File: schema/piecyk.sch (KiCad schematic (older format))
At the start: 29 parts, among them IC1 ATMEGA8-AI, P1 PWR_IN, P2 PWR_OUT, P3 CONN_01X04, P4 CONN_01X04, P5 ISP_IDC, Q1 2N7002, Q2 2N7002, Q3 BC516, SW1 SW_edit, SW2 SW_up, SW3 SW_down, U1 78L05, U2 LM35, U3 HD44780

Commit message: Add 10uF capacitor, optimalize PCB layout
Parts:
- added C3: 10u, Capacitors_Tantalum_SMD:TantalC_SizeA_EIA-3216_HandSoldering, symbol CAPAPOL
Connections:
- net +5V: now also C3.1
- net GND: now also C3.2
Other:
- moved on the sheet: C2
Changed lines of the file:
@@
 $EndComp
 $Comp
-L GND #PWR11
+L GND #PWR01
 U 1 1 52BB03AA
 P 3700 2000
-F 0 "#PWR11" H 3700 2000 30  0001 C CNN
+F 0 "#PWR01" H 3700 2000 30  0001 C CNN
 F 1 "GND" H 3700 1930 30  0001 C CNN
 F 2 "" H 3700 2000 60  0000 C CNN
@@
 $EndComp
 $Comp
-L GND #PWR4
+L GND #PWR02
 U 1 1 52BB0515
 P 1350 4650
-F 0 "#PWR4" H 1350 4650 30  0001 C CNN
+F 0 "#PWR02" H 1350 4650 30  0001 C CNN
 F 1 "GND" H 1350 4580 30  0001 C CNN
 F 2 "" H 1350 4650 60  0000 C CNN
@@
 $EndComp
 $Comp
-L GND #PWR1
+L GND #PWR03
 U 1 1 52BB0524
 P 1050 4650
-F 0 "#PWR1" H 1050 4650 30  0001 C CNN
+F 0 "#PWR03" H 1050 4650 30  0001 C CNN
 F 1 "GND" H 1050 4580 30  0001 C CNN
 F 2 "" H 1050 4650 60  0000 C CNN
@@
 $EndComp
 $Comp
-L GND #PWR5
+L GND #PWR04
 U 1 1 52BB0533
 P 1550 4650
-F 0 "#PWR5" H 1550 4650 30  0001 C CNN
+F 0 "#PWR04" H 1550 4650 30  0001 C CNN
 F 1 "GND" H 1550 4580 30  0001 C CNN
 F 2 "" H 1550 4650 60  0000 C CNN
@@
 $EndComp
 $Comp
-L GND #PWR10
+L GND #PWR05
 U 1 1 52BB0800
 P 3150 6450
-F 0 "#PWR10" H 3150 6450 30  0001 C CNN
+F 0 "#PWR05" H 3150 6450 30  0001 C CNN
 F 1 "GND" H 3150 6380 30  0001 C CNN
 F 2 "" H 3150 6450 60  0000 C CNN
@@
 $EndComp
 $Comp
-L +12V #PWR9
+L +12V #PWR06
 U 1 1 52D0DF48
 P 2950 950
-F 0 "#PWR9" H 2950 900 20  0001 C CNN
+F 0 "#PWR06" H 2950 900 20  0001 C CNN
 F 1 "+12V" H 2950 1050 30  0000 C CNN
 F 2 "" H 2950 950 60  0000 C CNN
@@
 $EndComp
 $Comp
-L GND #PWR15
+L GND #PWR07
 U 1 1 52D0FAD8
 P 6200 3150
-F 0 "#PWR15" H 6200 3150 30  0001 C CNN
+F 0 "#PWR07" H 6200 3150 30  0001 C CNN
 F 1 "GND" H 6200 3080 30  0001 C CNN
 F 2 "" H 6200 3150 60  0000 C CNN
@@
 $EndComp
 $Comp
-L GND #PWR6
+L GND #PWR08
 U 1 1 5459316E
 P 1750 1450
-F 0 "#PWR6" H 1750 1450 30  0001 C CNN
+F 0 "#PWR08" H 1750 1450 30  0001 C CNN
 F 1 "GND" H 1750 1380 30  0001 C CNN
 F 2 "" H 1750 1450 60  0000 C CNN
@@
 $EndComp
 $Comp
-L GND #PWR24
+L GND #PWR09
 U 1 1 54594AD7
 P 9400 2650
-F 0 "#PWR24" H 9400 2650 30  0001 C CNN
+F 0 "#PWR09" H 9400 2650 30  0001 C CNN
 F 1 "GND" H 9400 2580 30  0001 C CNN
 F 2 "" H 9400 2650 60  0000 C CNN
@@
 L C C2
 U 1 1 52BB0288
-P 4200 1450
-F 0 "C2" H 4200 1550 40  0000 L CNN
-F 1 "100n" H 4206 1365 40  0000 L CNN
-F 2 "Capacitors_SMD:C_0805_HandSoldering" H 4238 1300 30  0000 C CNN
-F 3 "~" H 4200 1450 60  0000 C CNN
-	1    4200 1450
+P 4450 1450
+F 0 "C2" H 4450 1550 40  0000 L CNN
+F 1 "100n" H 4456 1365 40  0000 L CNN
+F 2 "Capacitors_SMD:C_0805_HandSoldering" H 4488 1300 30  0000 C CNN
+F 3 "~" H 4450 1450 60  0000 C CNN
+	1    4450 1450
 	1    0    0    -1
 $EndComp
@@
 	3150 1650 3150 1750
 Wire Wire Line
-	3150 1750 4200 1750
+	3150 1750 4450 1750
 Connection ~ 3700 1750
 Wire Wire Line
@@
 	2950 950  2950 1150
 Wire Wire Line
-	4450 1150 4450 950
-$Comp
-L +5V #PWR12
+	4450 950  4450 1250
+$Comp
+L +5V #PWR010
 U 1 1 548A0516
 P 4450 950
-F 0 "#PWR12" H 4450 1040 20  0001 C CNN
+F 0 "#PWR010" H 4450 1040 20  0001 C CNN
 F 1 "+5V" H 4450 1040 30  0000 C CNN
 F 2 "" H 4450 950 60  0000 C CNN
@@
 LCD_RS
 $Comp
-L +5V #PWR23
+L +5V #PWR011
 U 1 1 548A0D87
 P 9100 2350
-F 0 "#PWR23" H 9100 2440 20  0001 C CNN
+F 0 "#PWR011" H 9100 2440 20  0001 C CNN
 F 1 "+5V" H 9100 2440 30  0000 C CNN
 F 2 "" H 9100 2350 60  0000 C CNN
@@
 $EndComp
 $Comp
-L +5V #PWR3
+L +5V #PWR012
 U 1 1 548A102B
 P 1300 2700
-F 0 "#PWR3" H 1300 2790 20  0001 C CNN
+F 0 "#PWR012" H 1300 2790 20  0001 C CNN
 F 1 "+5V" H 1300 2790 30  0000 C CNN
 F 2 "" H 1300 2700 60  0000 C CNN
@@
 $EndComp
 $Comp
-L GND #PWR13
+L GND #PWR013
 U 1 1 548A1F87
 P 5100 5800
-F 0 "#PWR13" H 5100 5800 30  0001 C CNN
+F 0 "#PWR013" H 5100 5800 30  0001 C CNN
 F 1 "GND" H 5100 5730 30  0001 C CNN
 F 2 "" H 5100 5800 60  0000 C CNN
@@
 	6300 7650 5250 7650
 $Comp
-L +12V #PWR2
+L +12V #PWR014
 U 1 1 548A221E
 P 1300 1300
-F 0 "#PWR2" H 1300 1250 20  0001 C CNN
+F 0 "#PWR014" H 1300 1250 20  0001 C CNN
 F 1 "+12V" H 1300 1400 30  0000 C CNN
 F 2 "" H 1300 1300 60  0000 C CNN
@@
 	8250 5650 8450 5650
 $Comp
-L GND #PWR19
+L GND #PWR015
 U 1 1 548A2843
 P 8250 5800
-F 0 "#PWR19" H 8250 5800 30  0001 C CNN
+F 0 "#PWR015" H 8250 5800 30  0001 C CNN
 F 1 "GND" H 8250 5730 30  0001 C CNN
 F 2 "" H 8250 5800 60  0000 C CNN
@@
 	8250 5800 8250 5650
 $Comp
-L +5V #PWR14
+L +5V #PWR016
 U 1 1 548A2D1F
 P 5150 2750
-F 0 "#PWR14" H 5150 2840 20  0001 C CNN
+F 0 "#PWR016" H 5150 2840 20  0001 C CNN
 F 1 "+5V" H 5150 2840 30  0000 C CNN
 F 2 "" H 5150 2750 60  0000 C CNN
@@
 	8100 4500 8100 5450
 $Comp
-L +12V #PWR18
+L +12V #PWR017
 U 1 1 548A3482
 P 8100 3400
-F 0 "#PWR18" H 8100 3350 20  0001 C CNN
+F 0 "#PWR017" H 8100 3350 20  0001 C CNN
 F 1 "+12V" H 8100 3500 30  0000 C CNN
 F 2 "" H 8100 3400 60  0000 C CNN
@@
 	7150 4850 7150 4950
 $Comp
-L GND #PWR16
+L GND #PWR018
 U 1 1 548A3B00
 P 7150 5550
-F 0 "#PWR16" H 7150 5550 30  0001 C CNN
+F 0 "#PWR018" H 7150 5550 30  0001 C CNN
 F 1 "GND" H 7150 5480 30  0001 C CNN
 F 2 "" H 7150 5550 60  0000 C CNN
@@
 	7950 950  7950 1050
 $Comp
-L GND #PWR17
+L GND #PWR019
 U 1 1 548A6D90
 P 7950 1650
-F 0 "#PWR17" H 7950 1650 30  0001 C CNN
+F 0 "#PWR019" H 7950 1650 30  0001 C CNN
 F 1 "GND" H 7950 1580 30  0001 C CNN
 F 2 "" H 7950 1650 60  0000 C CNN
@@
 $EndComp
 $Comp
-L +5V #PWR20
+L +5V #PWR020
 U 1 1 548A7182
 P 8450 1800
-F 0 "#PWR20" H 8450 1890 20  0001 C CNN
+F 0 "#PWR020" H 8450 1890 20  0001 C CNN
 F 1 "+5V" H 8450 1890 30  0000 C CNN
 F 2 "" H 8450 1800 60  0000 C CNN
@@
 	8450 1800 8450 1950
 $Comp
-L GND #PWR21
+L GND #PWR021
 U 1 1 548A73F6
 P 8450 2650
-F 0 "#PWR21" H 8450 2650 30  0001 C CNN
+F 0 "#PWR021" H 8450 2650 30  0001 C CNN
 F 1 "GND" H 8450 2580 30  0001 C CNN
 F 2 "" H 8450 2650 60  0000 C CNN
@@
 NoConn ~ 9500 1850
 $Comp
-L +5V #PWR22
+L +5V #PWR022
 U 1 1 548A85D9
 P 8800 1050
-F 0 "#PWR22" H 8800 1140 20  0001 C CNN
+F 0 "#PWR022" H 8800 1140 20  0001 C CNN
 F 1 "+5V" H 8800 1140 30  0000 C CNN
 F 2 "" H 8800 1050 60  0000 C CNN
@@
 Connection ~ 2000 6850
 $Comp
-L GND #PWR8
+L GND #PWR023
 U 1 1 548AA223
 P 2000 7250
-F 0 "#PWR8" H 2000 7250 30  0001 C CNN
+F 0 "#PWR023" H 2000 7250 30  0001 C CNN
 F 1 "GND" H 2000 7180 30  0001 C CNN
 F 2 "" H 2000 7250 60  0000 C CNN
@@
 $EndComp
 $Comp
-L +5V #PWR7
+L +5V #PWR024
 U 1 1 548AA403
 P 2000 6550
-F 0 "#PWR7" H 2000 6640 20  0001 C CNN
+F 0 "#PWR024" H 2000 6640 20  0001 C CNN
 F 1 "+5V" H 2000 6640 30  0000 C CNN
 F 2 "" H 2000 6550 60  0000 C CNN
@@
 Text Label 1200 6950 2    60   ~ 0
 SCK
+Connection ~ 4450 1150
+Wire Wire Line
+	4450 1750 4450 1650
+Connection ~ 4200 1750
+$Comp
+L CAPAPOL C3
+U 1 1 548A40D8
+P 4200 1450
+F 0 "C3" H 4250 1550 40  0000 L CNN
+F 1 "10u" H 4250 1350 40  0000 L CNN
+F 2 "Capacitors_Tantalum_SMD:TantalC_SizeA_EIA-3216_HandSoldering" H 4300 1300 30  0001 C CNN
+F 3 "" H 4200 1450 300 0000 C CNN
+	1    4200 1450
+	1    0    0    -1
+$EndComp
 $EndSCHEMATC

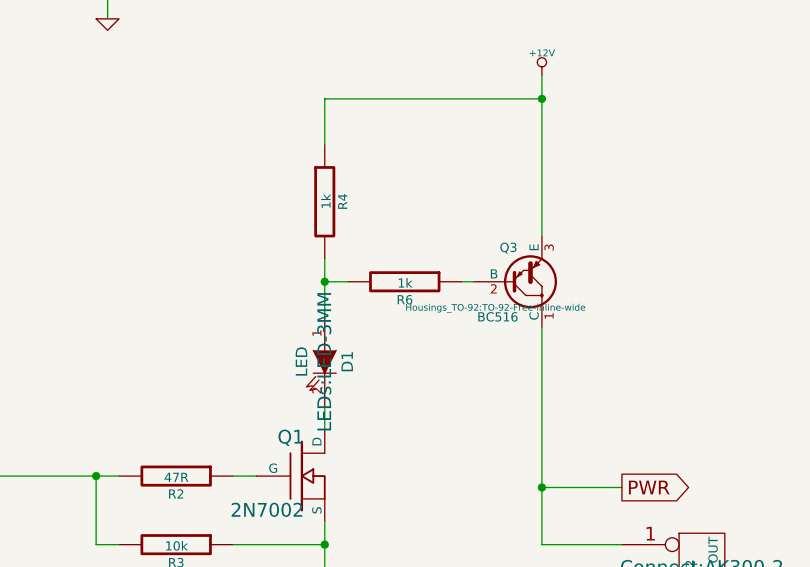
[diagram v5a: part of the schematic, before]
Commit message: Change resistor from 1k to 2k2 to limit base current
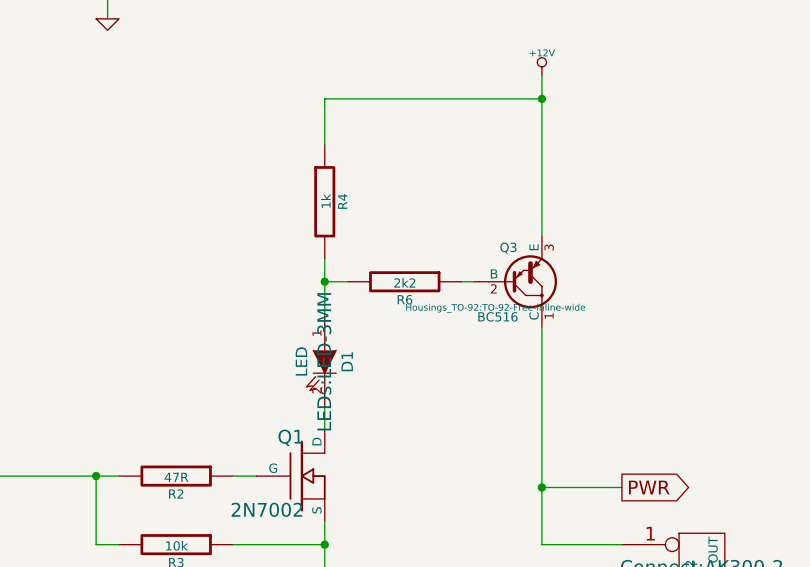
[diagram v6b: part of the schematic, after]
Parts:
- R6: value 1k -> 2k2
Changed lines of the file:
@@
 P 7500 4300
 F 0 "R6" V 7580 4300 40  0000 C CNN
-F 1 "1k" V 7507 4301 40  0000 C CNN
+F 1 "2k2" V 7507 4301 40  0000 C CNN
 F 2 "Resistors_SMD:R_0805_HandSoldering" V 7430 4300 30  0001 C CNN
 F 3 "" H 7500 4300 30  0000 C CNN

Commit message: Remove local libraries as the components are merged upstream
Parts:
- U2: footprint Discret:TO92-123 -> (none)
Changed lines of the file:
@@
 LIBS:valves
 LIBS:atmel
-LIBS:lm35
 LIBS:piecyk-cache
 EELAYER 25 0
@@
 $EndComp
 $Comp
-L GND #PWR01
+L GND #PWR11
 U 1 1 52BB03AA
 P 3700 2000
-F 0 "#PWR01" H 3700 2000 30  0001 C CNN
+F 0 "#PWR11" H 3700 2000 30  0001 C CNN
 F 1 "GND" H 3700 1930 30  0001 C CNN
 F 2 "" H 3700 2000 60  0000 C CNN
@@
 $EndComp
 $Comp
-L GND #PWR02
+L GND #PWR4
 U 1 1 52BB0515
 P 1350 4650
-F 0 "#PWR02" H 1350 4650 30  0001 C CNN
+F 0 "#PWR4" H 1350 4650 30  0001 C CNN
 F 1 "GND" H 1350 4580 30  0001 C CNN
 F 2 "" H 1350 4650 60  0000 C CNN
@@
 $EndComp
 $Comp
-L GND #PWR03
+L GND #PWR1
 U 1 1 52BB0524
 P 1050 4650
-F 0 "#PWR03" H 1050 4650 30  0001 C CNN
+F 0 "#PWR1" H 1050 4650 30  0001 C CNN
 F 1 "GND" H 1050 4580 30  0001 C CNN
 F 2 "" H 1050 4650 60  0000 C CNN
@@
 $EndComp
 $Comp
-L GND #PWR04
+L GND #PWR5
 U 1 1 52BB0533
 P 1550 4650
-F 0 "#PWR04" H 1550 4650 30  0001 C CNN
+F 0 "#PWR5" H 1550 4650 30  0001 C CNN
 F 1 "GND" H 1550 4580 30  0001 C CNN
 F 2 "" H 1550 4650 60  0000 C CNN
@@
 $EndComp
 $Comp
-L GND #PWR05
+L GND #PWR10
 U 1 1 52BB0800
 P 3150 6450
-F 0 "#PWR05" H 3150 6450 30  0001 C CNN
+F 0 "#PWR10" H 3150 6450 30  0001 C CNN
 F 1 "GND" H 3150 6380 30  0001 C CNN
 F 2 "" H 3150 6450 60  0000 C CNN
@@
 $EndComp
 $Comp
-L +12V #PWR06
+L +12V #PWR9
 U 1 1 52D0DF48
 P 2950 950
-F 0 "#PWR06" H 2950 900 20  0001 C CNN
+F 0 "#PWR9" H 2950 900 20  0001 C CNN
 F 1 "+12V" H 2950 1050 30  0000 C CNN
 F 2 "" H 2950 950 60  0000 C CNN
@@
 $EndComp
 $Comp
-L GND #PWR07
+L GND #PWR15
 U 1 1 52D0FAD8
 P 6200 3150
-F 0 "#PWR07" H 6200 3150 30  0001 C CNN
+F 0 "#PWR15" H 6200 3150 30  0001 C CNN
 F 1 "GND" H 6200 3080 30  0001 C CNN
 F 2 "" H 6200 3150 60  0000 C CNN
@@
 $EndComp
 $Comp
-L GND #PWR08
+L GND #PWR6
 U 1 1 5459316E
 P 1750 1450
-F 0 "#PWR08" H 1750 1450 30  0001 C CNN
+F 0 "#PWR6" H 1750 1450 30  0001 C CNN
 F 1 "GND" H 1750 1380 30  0001 C CNN
 F 2 "" H 1750 1450 60  0000 C CNN
@@
 $EndComp
 $Comp
-L GND #PWR09
+L GND #PWR24
 U 1 1 54594AD7
 P 9400 2650
-F 0 "#PWR09" H 9400 2650 30  0001 C CNN
+F 0 "#PWR24" H 9400 2650 30  0001 C CNN
 F 1 "GND" H 9400 2580 30  0001 C CNN
 F 2 "" H 9400 2650 60  0000 C CNN
@@
 	1    9400 2650
 	1    0    0    -1
-$EndComp
-$Comp
-L LM35 U2
-U 1 1 5489DA5C
-P 5700 2850
-F 0 "U2" H 5350 2900 60  0000 C CNN
-F 1 "LM35" H 5350 2800 60  0000 C CNN
-F 2 "Discret:TO92-123" H 5700 3100 60  0001 C CNN
-F 3 "" H 5700 3100 60  0000 C CNN
-	1    5700 2850
-	0    -1   1    0
 $EndComp
 $Comp
@@
 	4450 950  4450 1250
 $Comp
-L +5V #PWR010
+L +5V #PWR12
 U 1 1 548A0516
 P 4450 950
-F 0 "#PWR010" H 4450 1040 20  0001 C CNN
+F 0 "#PWR12" H 4450 1040 20  0001 C CNN
 F 1 "+5V" H 4450 1040 30  0000 C CNN
 F 2 "" H 4450 950 60  0000 C CNN
@@
 LCD_RS
 $Comp
-L +5V #PWR011
+L +5V #PWR23
 U 1 1 548A0D87
 P 9100 2350
-F 0 "#PWR011" H 9100 2440 20  0001 C CNN
+F 0 "#PWR23" H 9100 2440 20  0001 C CNN
 F 1 "+5V" H 9100 2440 30  0000 C CNN
 F 2 "" H 9100 2350 60  0000 C CNN
@@
 $EndComp
 $Comp
-L +5V #PWR012
+L +5V #PWR3
 U 1 1 548A102B
 P 1300 2700
-F 0 "#PWR012" H 1300 2790 20  0001 C CNN
+F 0 "#PWR3" H 1300 2790 20  0001 C CNN
 F 1 "+5V" H 1300 2790 30  0000 C CNN
 F 2 "" H 1300 2700 60  0000 C CNN
@@
 $EndComp
 $Comp
-L GND #PWR013
+L GND #PWR13
 U 1 1 548A1F87
 P 5100 5800
-F 0 "#PWR013" H 5100 5800 30  0001 C CNN
+F 0 "#PWR13" H 5100 5800 30  0001 C CNN
 F 1 "GND" H 5100 5730 30  0001 C CNN
 F 2 "" H 5100 5800 60  0000 C CNN
@@
 	6300 7650 5250 7650
 $Comp
-L +12V #PWR014
+L +12V #PWR2
 U 1 1 548A221E
 P 1300 1300
-F 0 "#PWR014" H 1300 1250 20  0001 C CNN
+F 0 "#PWR2" H 1300 1250 20  0001 C CNN
 F 1 "+12V" H 1300 1400 30  0000 C CNN
 F 2 "" H 1300 1300 60  0000 C CNN
@@
 	8250 5650 8450 5650
 $Comp
-L GND #PWR015
+L GND #PWR19
 U 1 1 548A2843
 P 8250 5800
-F 0 "#PWR015" H 8250 5800 30  0001 C CNN
+F 0 "#PWR19" H 8250 5800 30  0001 C CNN
 F 1 "GND" H 8250 5730 30  0001 C CNN
 F 2 "" H 8250 5800 60  0000 C CNN
@@
 	8250 5800 8250 5650
 $Comp
-L +5V #PWR016
+L +5V #PWR14
 U 1 1 548A2D1F
 P 5150 2750
-F 0 "#PWR016" H 5150 2840 20  0001 C CNN
+F 0 "#PWR14" H 5150 2840 20  0001 C CNN
 F 1 "+5V" H 5150 2840 30  0000 C CNN
 F 2 "" H 5150 2750 60  0000 C CNN
@@
 	8100 4500 8100 5450
 $Comp
-L +12V #PWR017
+L +12V #PWR18
 U 1 1 548A3482
 P 8100 3400
-F 0 "#PWR017" H 8100 3350 20  0001 C CNN
+F 0 "#PWR18" H 8100 3350 20  0001 C CNN
 F 1 "+12V" H 8100 3500 30  0000 C CNN
 F 2 "" H 8100 3400 60  0000 C CNN
@@
 	7150 4850 7150 4950
 $Comp
-L GND #PWR018
+L GND #PWR16
 U 1 1 548A3B00
 P 7150 5550
-F 0 "#PWR018" H 7150 5550 30  0001 C CNN
+F 0 "#PWR16" H 7150 5550 30  0001 C CNN
 F 1 "GND" H 7150 5480 30  0001 C CNN
 F 2 "" H 7150 5550 60  0000 C CNN
@@
 	7950 950  7950 1050
 $Comp
-L GND #PWR019
+L GND #PWR17
 U 1 1 548A6D90
 P 7950 1650
-F 0 "#PWR019" H 7950 1650 30  0001 C CNN
+F 0 "#PWR17" H 7950 1650 30  0001 C CNN
 F 1 "GND" H 7950 1580 30  0001 C CNN
 F 2 "" H 7950 1650 60  0000 C CNN
@@
 $EndComp
 $Comp
-L +5V #PWR020
+L +5V #PWR20
 U 1 1 548A7182
 P 8450 1800
-F 0 "#PWR020" H 8450 1890 20  0001 C CNN
+F 0 "#PWR20" H 8450 1890 20  0001 C CNN
 F 1 "+5V" H 8450 1890 30  0000 C CNN
 F 2 "" H 8450 1800 60  0000 C CNN
@@
 	8450 1800 8450 1950
 $Comp
-L GND #PWR021
+L GND #PWR21
 U 1 1 548A73F6
 P 8450 2650
-F 0 "#PWR021" H 8450 2650 30  0001 C CNN
+F 0 "#PWR21" H 8450 2650 30  0001 C CNN
 F 1 "GND" H 8450 2580 30  0001 C CNN
 F 2 "" H 8450 2650 60  0000 C CNN
@@
 NoConn ~ 9500 1850
 $Comp
-L +5V #PWR022
+L +5V #PWR22
 U 1 1 548A85D9
 P 8800 1050
-F 0 "#PWR022" H 8800 1140 20  0001 C CNN
+F 0 "#PWR22" H 8800 1140 20  0001 C CNN
 F 1 "+5V" H 8800 1140 30  0000 C CNN
 F 2 "" H 8800 1050 60  0000 C CNN
@@
 Connection ~ 2000 6850
 $Comp
-L GND #PWR023
+L GND #PWR8
 U 1 1 548AA223
 P 2000 7250
-F 0 "#PWR023" H 2000 7250 30  0001 C CNN
+F 0 "#PWR8" H 2000 7250 30  0001 C CNN
 F 1 "GND" H 2000 7180 30  0001 C CNN
 F 2 "" H 2000 7250 60  0000 C CNN
@@
 $EndComp
 $Comp
-L +5V #PWR024
+L +5V #PWR7
 U 1 1 548AA403
 P 2000 6550
-F 0 "#PWR024" H 2000 6640 20  0001 C CNN
+F 0 "#PWR7" H 2000 6640 20  0001 C CNN
 F 1 "+5V" H 2000 6640 30  0000 C CNN
 F 2 "" H 2000 6550 60  0000 C CNN
@@
 	1    0    0    -1
 $EndComp
+$Comp
+L LM35 U2
+U 1 1 548BE2A8
+P 5700 2850
+F 0 "U2" H 5350 2900 60  0000 C CNN
+F 1 "LM35" H 5350 2800 60  0000 C CNN
+F 2 "" H 5700 3100 60  0000 C CNN
+F 3 "" H 5700 3100 60  0000 C CNN
+	1    5700 2850
+	0    -1   1    0
+$EndComp
 $EndSCHEMATC
